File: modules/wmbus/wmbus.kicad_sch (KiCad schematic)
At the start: 9 parts

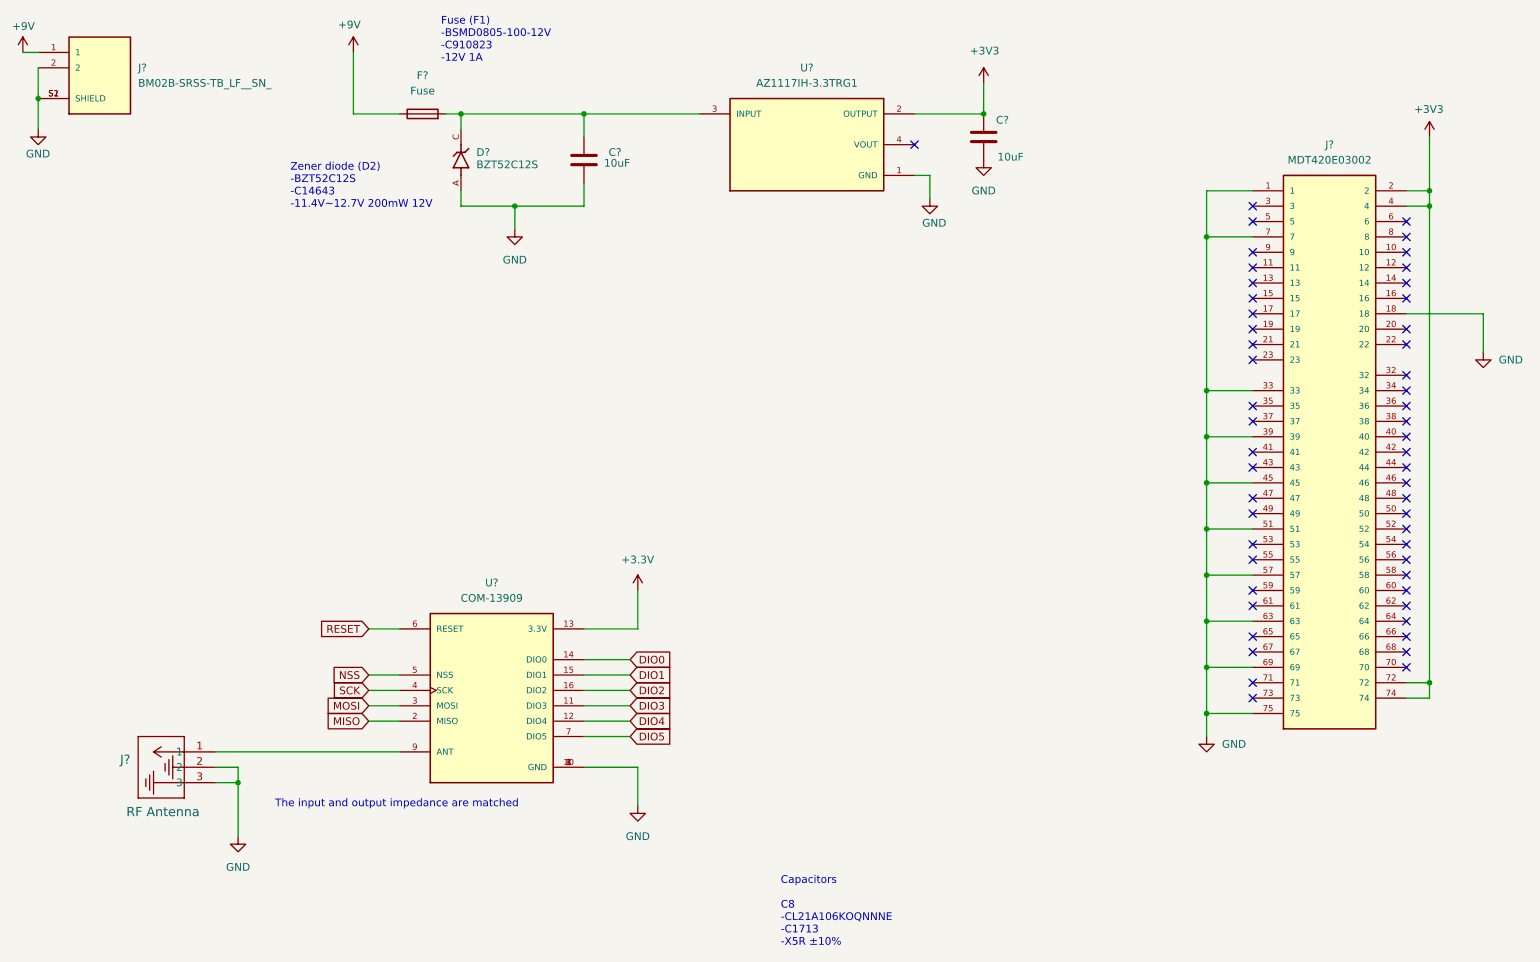
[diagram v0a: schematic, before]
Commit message: fix: routing mbus
Signed-off-by: Rodney Osodo <socials@rodneyosodo.com>
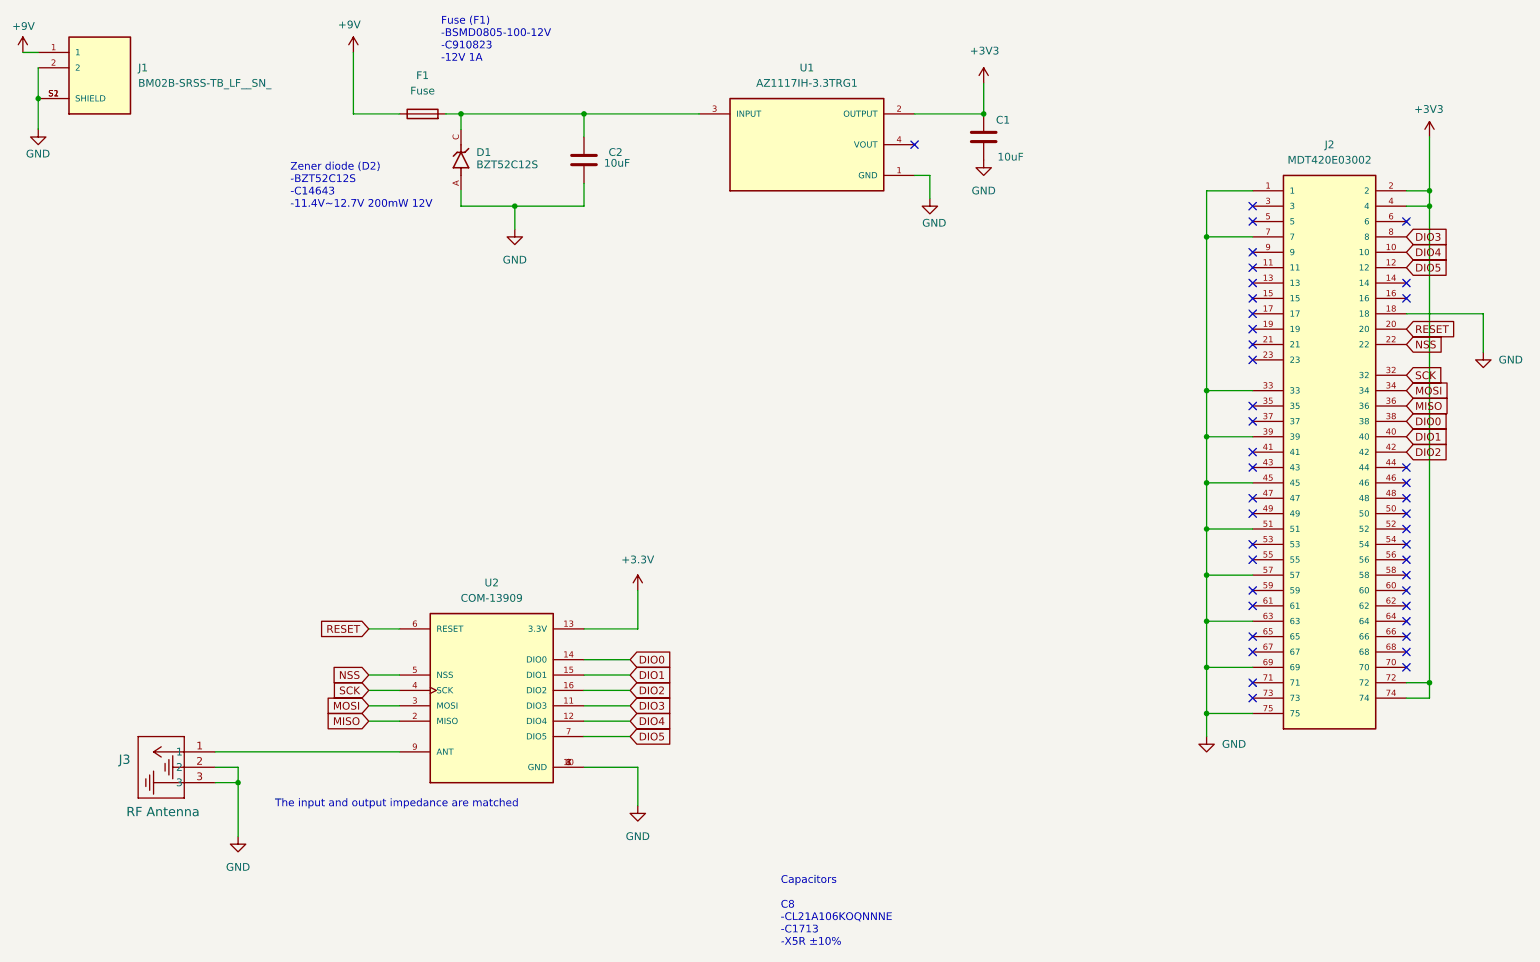
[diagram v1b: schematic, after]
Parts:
- J3: renamed from J?; footprint CONUFL001_SMD_T:CONN1_CONUFL_TEC -> CONUFL001_SMD_T:LINX_CONUFL001-SMD-T
- gave numbers to parts that had none: 8
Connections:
- net DIO0: now also J2.38
- net DIO1: now also J2.40
- net DIO2: now also J2.42
- net DIO3: now also J2.8
- net DIO4: now also J2.10
- net DIO5: now also J2.12
- net MISO: now also J2.36
- net MOSI: now also J2.34
- net NSS: now also J2.22
- net RESET: now also J2.20
- net SCK: now also J2.32
- no-connect marks 53 -> 42
